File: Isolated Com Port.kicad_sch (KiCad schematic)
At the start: 0 parts

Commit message: Added FT231XQ USB to UART IC
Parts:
- added U1: FT231XQ, Package_DFN_QFN:QFN-20-1EP_4x4mm_P0.5mm_EP2.5x2.5mm, symbol Interface_USB:FT231XQ
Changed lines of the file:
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@@
 	(generator_version "8.0")
 	(paper "A4")
+	(symbol
+		(lib_id "Interface_USB:FT231XQ")
+		(at 148.59 106.68 0)
+		(unit 1)
+		(exclude_from_sim no)
+		(in_bom yes)
+		(on_board yes)
+		(dnp no)
+		(fields_autoplaced yes)
+		(property "Reference" "U1"
+			(at 153.3241 83.82 0)
+			(effects
+				(font
+					(size 1.27 1.27)
+				)
+				(justify left)
+			)
+		)
+		(property "Value" "FT231XQ"
+			(at 153.3241 86.36 0)
+			(effects
+				(font
+					(size 1.27 1.27)
+				)
+				(justify left)
+			)
+		)
+		(property "Footprint" "Package_DFN_QFN:QFN-20-1EP_4x4mm_P0.5mm_EP2.5x2.5mm"
+			(at 182.88 127 0)
+			(effects
+				(font
+					(size 1.27 1.27)
+				)
+				(hide yes)
+			)
+		)
+		(property "Datasheet" "https://www.ftdichip.com/Support/Documents/DataSheets/ICs/DS_FT231X.pdf"
+			(at 148.59 106.68 0)
+			(effects
+				(font
+					(size 1.27 1.27)
+				)
+				(hide yes)
+			)
+		)
+		(property "Description" "Full Speed USB to Full Handshake UART, QFN-20"
+			(at 148.59 106.68 0)
+			(effects
+				(font
+					(size 1.27 1.27)
+				)
+				(hide yes)
+			)
+		)
+		(pin "9"
+		)
+		(pin "1"
+		)
+		(pin "2"
+		)
+		(pin "5"
+		)
+		(pin "16"
+		)
+		(pin "17"
+		)
+		(pin "19"
+		)
+		(pin "4"
+		)
+		(pin "14"
+		)
+		(pin "15"
+		)
+		(pin "11"
+		)
+		(pin "20"
+		)
+		(pin "21"
+		)
+		(pin "10"
+		)
+		(pin "18"
+		)
+		(pin "6"
+		)
+		(pin "7"
+		)
+		(pin "12"
+		)
+		(pin "3"
+		)
+		(pin "8"
+		)
+		(pin "13"
+		)
+		(instances
+			(project "Isolated Com Port"
+				(path "/736fe05f-3e80-4c58-a4b9-c0a7b5ae4e97"
+					(reference "U1")
+					(unit 1)
+				)
+			)
+		)
+	)
 	(sheet_instances
 		(path "/"

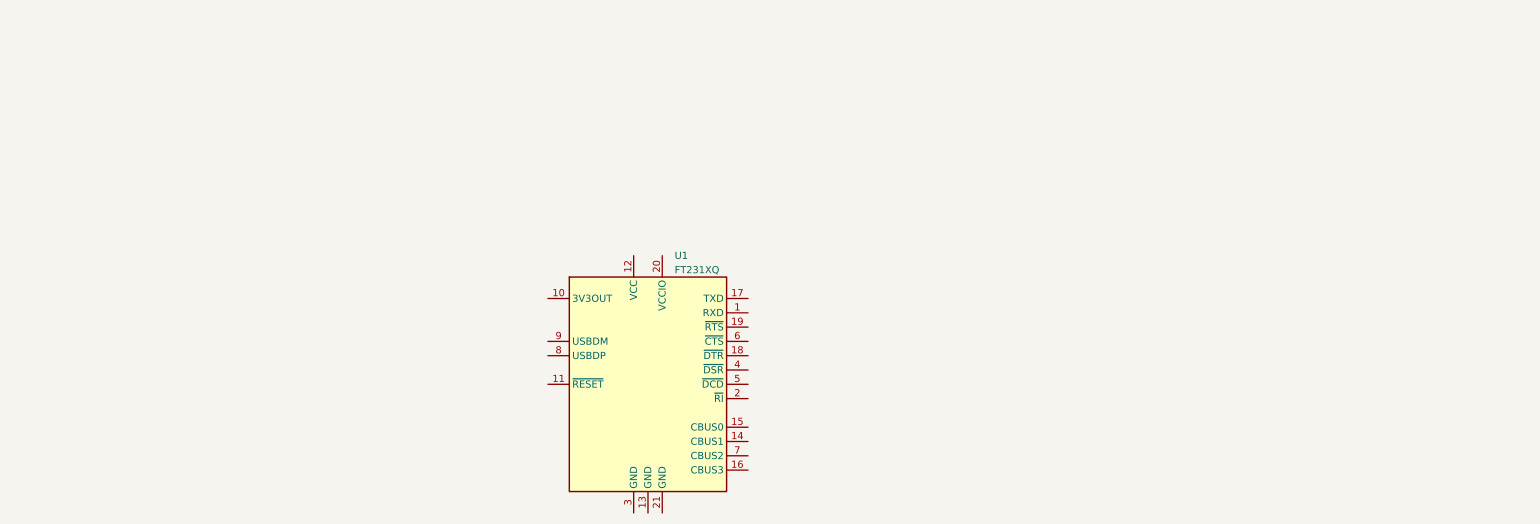
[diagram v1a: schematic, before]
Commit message: Added USB connectors and wired up USB-to-UART IC
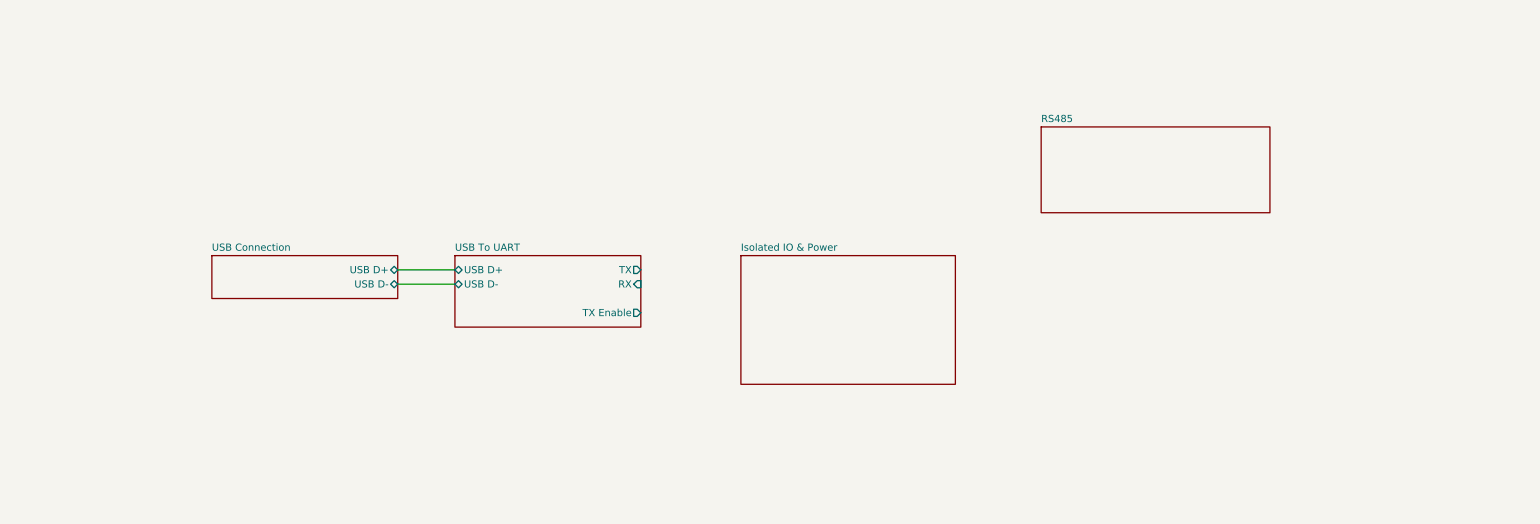
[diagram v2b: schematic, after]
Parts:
- removed U1: FT231XQ, Package_DFN_QFN:QFN-20-1EP_4x4mm_P0.5mm_EP2.5x2.5mm, symbol Interface_USB:FT231XQ
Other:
- added sheet Isolated IO & Power (Isolated IO & Power.kicad_sch)
- added sheet RS485 (RS485.kicad_sch)
- added sheet USB Connection (USB Connection.kicad_sch)
- added sheet USB To UART (USB To UART.kicad_sch)
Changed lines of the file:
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@@
 	(generator_version "8.0")
 	(paper "A4")
-	(symbol
-		(lib_id "Interface_USB:FT231XQ")
-		(at 148.59 106.68 0)
-		(unit 1)
-		(exclude_from_sim no)
-		(in_bom yes)
-		(on_board yes)
-		(dnp no)
-		(fields_autoplaced yes)
-		(property "Reference" "U1"
-			(at 153.3241 83.82 0)
+	(wire
+		(pts
+			(xy 104.14 88.9) (xy 114.3 88.9)
+		)
+		(stroke
+			(width 0)
+			(type default)
+		)
+	)
+	(wire
+		(pts
+			(xy 104.14 86.36) (xy 114.3 86.36)
+		)
+		(stroke
+			(width 0)
+			(type default)
+		)
+	)
+	(sheet
+		(at 114.3 83.82)
+		(size 33.02 12.7)
+		(fields_autoplaced yes)
+		(stroke
+			(width 0.1524)
+			(type solid)
+			(color 0 0 0 1)
+		)
+		(fill
+			(color 0 255 0 1.0000)
+		)
+		(property "Sheetname" "USB To UART"
+			(at 114.3 83.1084 0)
+			(effects
+				(font
+					(size 1.27 1.27)
+				)
+				(justify left bottom)
+			)
+		)
+		(property "Sheetfile" "USB To UART.kicad_sch"
+			(at 114.3 97.1046 0)
+			(effects
+				(font
+					(size 1.27 1.27)
+				)
+				(justify left top)
+				(hide yes)
+			)
+		)
+		(pin "USB D-" bidirectional
+			(at 114.3 88.9 180)
 			(effects
 				(font
@@
 			)
 		)
-		(property "Value" "FT231XQ"
-			(at 153.3241 86.36 0)
+		(pin "USB D+" bidirectional
+			(at 114.3 86.36 180)
 			(effects
 				(font
@@
 			)
 		)
-		(property "Footprint" "Package_DFN_QFN:QFN-20-1EP_4x4mm_P0.5mm_EP2.5x2.5mm"
-			(at 182.88 127 0)
-			(effects
-				(font
-					(size 1.27 1.27)
-				)
-				(hide yes)
-			)
-		)
-		(property "Datasheet" "https://www.ftdichip.com/Support/Documents/DataSheets/ICs/DS_FT231X.pdf"
-			(at 148.59 106.68 0)
-			(effects
-				(font
-					(size 1.27 1.27)
-				)
-				(hide yes)
-			)
-		)
-		(property "Description" "Full Speed USB to Full Handshake UART, QFN-20"
-			(at 148.59 106.68 0)
-			(effects
-				(font
-					(size 1.27 1.27)
-				)
-				(hide yes)
-			)
-		)
-		(pin "9"
-		)
-		(pin "1"
-		)
-		(pin "2"
-		)
-		(pin "5"
-		)
-		(pin "16"
-		)
-		(pin "17"
-		)
-		(pin "19"
-		)
-		(pin "4"
-		)
-		(pin "14"
-		)
-		(pin "15"
-		)
-		(pin "11"
-		)
-		(pin "20"
-		)
-		(pin "21"
-		)
-		(pin "10"
-		)
-		(pin "18"
-		)
-		(pin "6"
-		)
-		(pin "7"
-		)
-		(pin "12"
-		)
-		(pin "3"
-		)
-		(pin "8"
-		)
-		(pin "13"
-		)
-		(instances
-			(project "Isolated Com Port"
-				(path "/736fe05f-3e80-4c58-a4b9-c0a7b5ae4e97"
-					(reference "U1")
-					(unit 1)
-				)
-			)
+		(pin "TX Enable" output
+			(at 147.32 93.98 0)
+			(effects
+				(font
+					(size 1.27 1.27)
+				)
+				(justify right)
+			)
+		)
+		(pin "RX" input
+			(at 147.32 88.9 0)
+			(effects
+				(font
+					(size 1.27 1.27)
+				)
+				(justify right)
+			)
+		)
+		(pin "TX" output
+			(at 147.32 86.36 0)
+			(effects
+				(font
+					(size 1.27 1.27)
+				)
+				(justify right)
+			)
+		)
+		(instances
+			(project "Isolated Com Port"
+				(path "/736fe05f-3e80-4c58-a4b9-c0a7b5ae4e97"
+					(page "3")
+				)
+			)
+		)
+	)
+	(sheet
+		(at 165.1 83.82)
+		(size 38.1 22.86)
+		(fields_autoplaced yes)
+		(stroke
+			(width 0.1524)
+			(type solid)
+			(color 0 0 0 1)
+		)
+		(fill
+			(color 0 255 0 1.0000)
+		)
+		(property "Sheetname" "Isolated IO & Power"
+			(at 165.1 83.1084 0)
+			(effects
+				(font
+					(size 1.27 1.27)
+				)
+				(justify left bottom)
+			)
+		)
+		(property "Sheetfile" "Isolated IO & Power.kicad_sch"
+			(at 165.1 107.2646 0)
+			(effects
+				(font
+					(size 1.27 1.27)
+				)
+				(justify left top)
+				(hide yes)
+			)
+		)
+		(instances
+			(project "Isolated Com Port"
+				(path "/736fe05f-3e80-4c58-a4b9-c0a7b5ae4e97"
+					(page "4")
+				)
+			)
+		)
+	)
+	(sheet
+		(at 218.44 60.96)
+		(size 40.64 15.24)
+		(fields_autoplaced yes)
+		(stroke
+			(width 0.1524)
+			(type solid)
+			(color 0 0 0 1)
+		)
+		(fill
+			(color 0 255 0 1.0000)
+		)
+		(property "Sheetname" "RS485"
+			(at 218.44 60.2484 0)
+			(effects
+				(font
+					(size 1.27 1.27)
+				)
+				(justify left bottom)
+			)
+		)
+		(property "Sheetfile" "RS485.kicad_sch"
+			(at 218.44 76.7846 0)
+			(effects
+				(font
+					(size 1.27 1.27)
+					(color 0 255 0 1)
+				)
+				(justify left top)
+				(hide yes)
+			)
+		)
+		(instances
+			(project "Isolated Com Port"
+				(path "/736fe05f-3e80-4c58-a4b9-c0a7b5ae4e97"
+					(page "5")
+				)
+			)
+		)
+	)
+	(sheet
+		(at 71.12 83.82)
+		(size 33.02 7.62)
+		(fields_autoplaced yes)
+		(stroke
+			(width 0.1524)
+			(type solid)
+			(color 0 0 0 1)
+		)
+		(fill
+			(color 0 255 0 1.0000)
+		)
+		(property "Sheetname" "USB Connection"
+			(at 71.12 83.1084 0)
+			(effects
+				(font
+					(size 1.27 1.27)
+				)
+				(justify left bottom)
+			)
+		)
+		(property "Sheetfile" "USB Connection.kicad_sch"
+			(at 71.12 92.0246 0)
+			(effects
+				(font
+					(size 1.27 1.27)
+				)
+				(justify left top)
+				(hide yes)
+			)
+		)
+		(pin "USB D-" bidirectional
+			(at 104.14 88.9 0)
+			(effects
+				(font
+					(size 1.27 1.27)
+				)
+				(justify right)
+			)
+		)
+		(pin "USB D+" bidirectional
+			(at 104.14 86.36 0)
+			(effects
+				(font
+					(size 1.27 1.27)
+				)
+				(justify right)
+			)
+		)
+		(instances
+			(project "Isolated Com Port"
+				(path "/736fe05f-3e80-4c58-a4b9-c0a7b5ae4e97"
+					(page "2")
+				)
+			)

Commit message: Finished capturing schematics
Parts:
- added J2: Conn_01x07_MountingPin, symbol Connector_Generic_MountingPin:Conn_01x07_MountingPin
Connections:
- new net 5VDC DUT: J2.1 (Pin_1)
- new net GND DUT: J2.7 (Pin_7)
- new net Level Changer RX/In Vlow: J2.6 (Pin_6)
- new net Level Changer RX/Ref Low: J2.4 (Pin_4)
- new net Level Changer TX/Out Vhigh: J2.5 (Pin_5)
- new net RS485/RS485+: J2.2 (Pin_2)
- new net RS485/RS485-: J2.3 (Pin_3)
- no-connect marks 0 -> 1
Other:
- sheet Isolated IO & Power renamed Isolated IO
- added sheet Isolated Power (Isolated Power.kicad_sch)
- added sheet Level Changer RX (Level Changer.kicad_sch)
- added sheet Level Changer TX (Level Changer.kicad_sch)
- sheet Isolated IO: file Isolated IO & Power.kicad_sch -> Isolated IO.kicad_sch
- sheet Isolated IO ports: added In1 A, In2 A, In3 A, In4 B, Out1 B, Out2 B, Out3 B, Out4 A, Power A, Power B; removed none
- sheet RS485 ports: added RS485+, RS485-, RX, TX, TX Enable, Termination; removed none
- sheet USB To UART ports: added GPIO; removed none
- note added: "1500V"

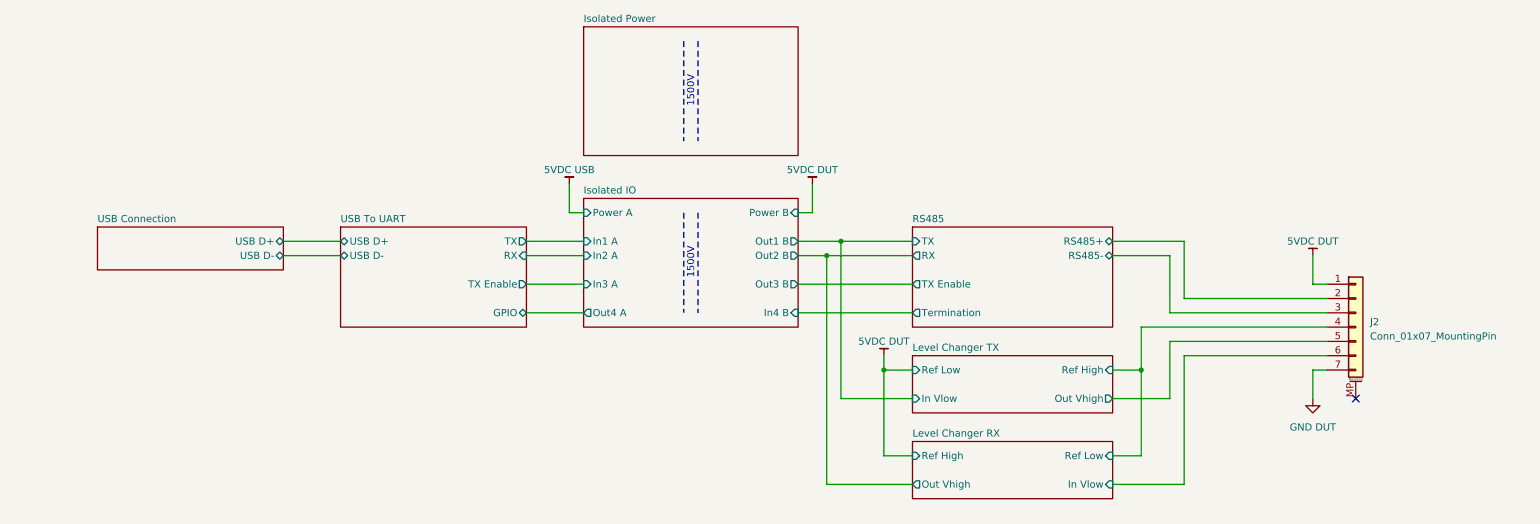
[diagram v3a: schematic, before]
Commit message: Power & Level Translation
Isolated 5VDC changed and a 3.3VDC LDO was added. The original 5VDC was too expensive and big. The new one is still both, but less so.
The level translator is now a dedicated IC instead of MOSFETs. I was having trouble making it work the way I wanted.
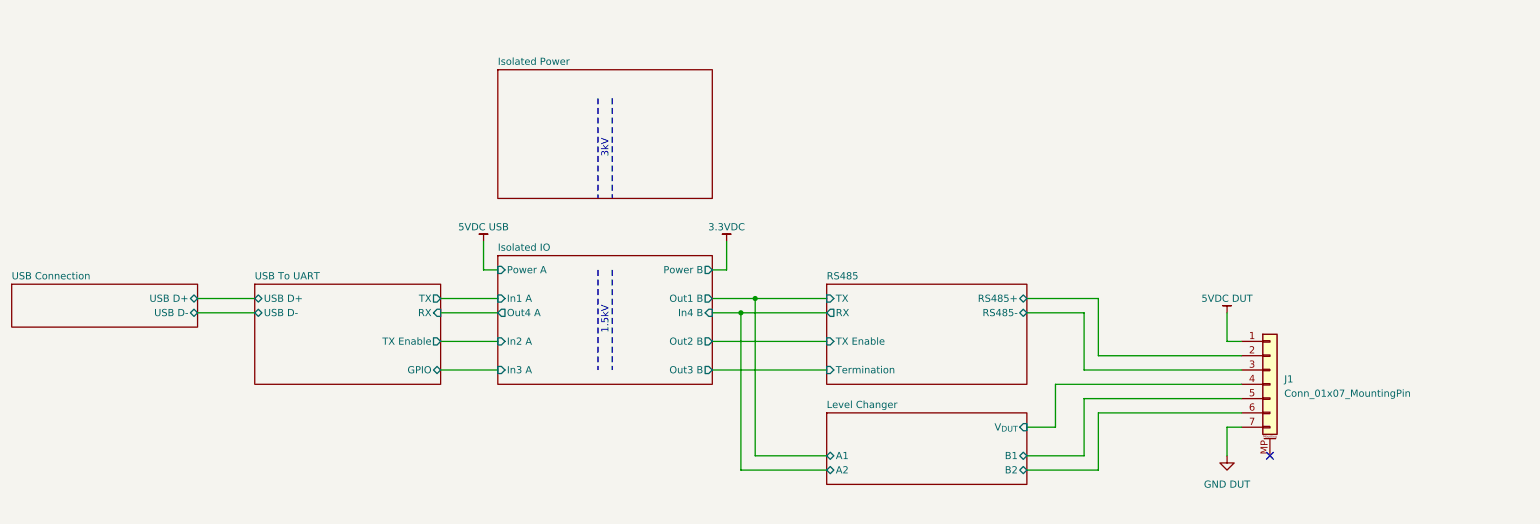
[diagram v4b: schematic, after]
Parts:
- renumbered J2 to J1
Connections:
- net Level Changer RX/In Vlow renamed Level Changer/B2
- net Level Changer RX/Ref Low renamed Level Changer/V_{DUT}
- net Level Changer/Out Vhigh renamed Level Changer/B1
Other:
- sheet Level Changer TX renamed Level Changer
- removed sheet Level Changer RX
- sheet Level Changer ports: added A1, A2, B1, B2, V_{DUT}; removed In Vlow, Out Vhigh, Ref High, Ref Low
- note added: "1.5kV"
- note added: "3kV"
- note removed: "1500V"
- moved on the sheet: J1
